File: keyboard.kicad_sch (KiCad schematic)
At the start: 27 parts, among them J2 Conn_01x05_Pin, SW1 SW_Push, U1 STM32F072C8Tx, U2 74AHCT1G125, U3 XC6206PxxxMR, U4 USB6B1

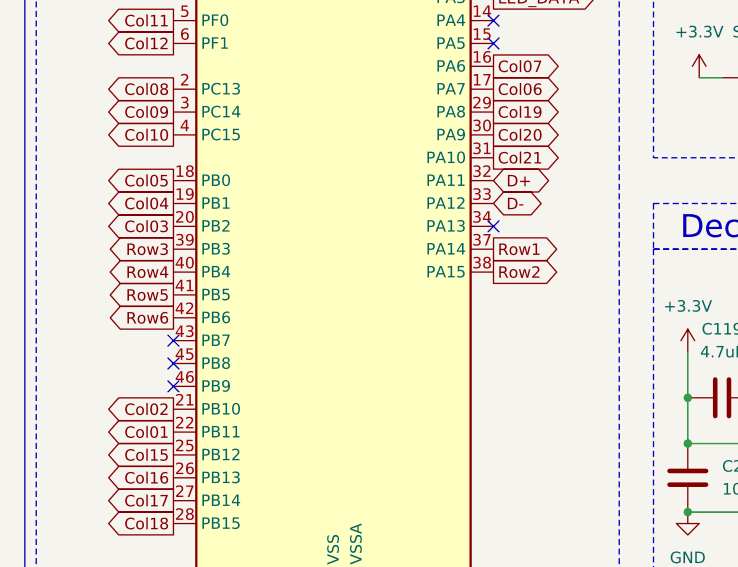
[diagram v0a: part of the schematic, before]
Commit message: Better LED 5V rail setup and matrix wiring
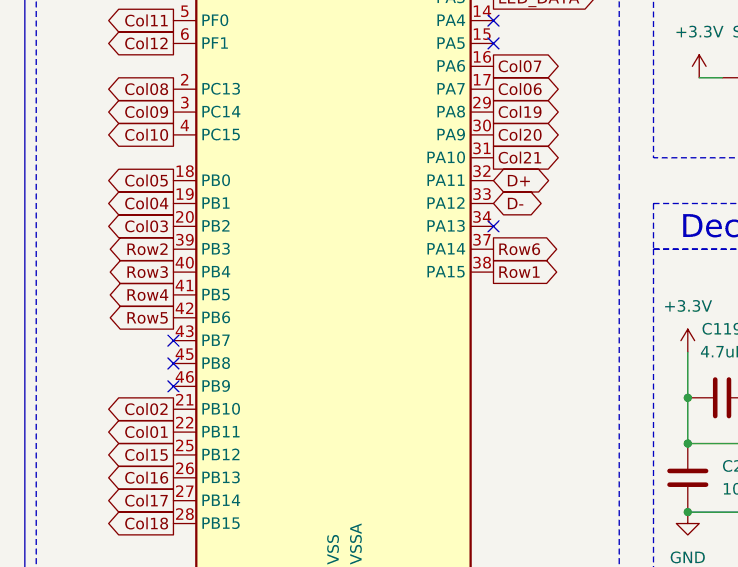
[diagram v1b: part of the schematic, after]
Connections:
- net Row1: now also U1.38 (PA15); no longer U1.37 (PA14)
- net Row2: now also U1.39 (PB3); no longer U1.38 (PA15)
- net Row3: now also U1.40 (PB4); no longer U1.39 (PB3)
- net Row4: now also U1.41 (PB5); no longer U1.40 (PB4)
- net Row5: now also U1.42 (PB6); no longer U1.41 (PB5)
- net Row6: now also U1.37 (PA14); no longer U1.42 (PB6)
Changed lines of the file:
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@@
+		)
+	)
+	(global_label "Row6"
+		(shape output)
+		(at 67.31 83.82 0)
+		(fields_autoplaced yes)
+		(effects
+			(font
+				(size 1.27 1.27)
+			)
+			(justify left)
+		)
+		(property "Intersheetrefs" "${INTERSHEET_REFS}"
+			(at 75.2542 83.82 0)
+			(hide yes)
+			(show_name no)
+			(do_not_autoplace no)
+			(effects
+				(font
+					(size 1.27 1.27)
+				)
+				(justify left)
+			)
 		)
 	)
@@
 		)
 	)
+	(global_label "Row5"
+		(shape output)
+		(at 31.75 91.44 180)
+		(fields_autoplaced yes)
+		(effects
+			(font
+				(size 1.27 1.27)
+			)
+			(justify right)
+		)
+		(property "Intersheetrefs" "${INTERSHEET_REFS}"
+			(at 23.8058 91.44 0)
+			(hide yes)
+			(show_name no)
+			(do_not_autoplace no)
+			(effects
+				(font
+					(size 1.27 1.27)
+				)
+				(justify right)
+			)
+		)
+	)
 	(global_label "Col16"
 		(shape output)
@@
 		)
 	)
+	(global_label "Col06"
+		(shape output)
+		(at 67.31 66.04 0)
+		(fields_autoplaced yes)
+		(effects
+			(font
+				(size 1.27 1.27)
+			)
+			(justify left)
+		)
+		(property "Intersheetrefs" "${INTERSHEET_REFS}"
+			(at 75.7984 66.04 0)
+			(hide yes)
+			(show_name no)
+			(do_not_autoplace no)
+			(effects
+				(font
+					(size 1.27 1.27)
+				)
+				(justify left)
+			)
+		)
+	)
+	(global_label "Col21"
+		(shape input)
+		(at 85.09 151.13 90)
+		(fields_autoplaced yes)
+		(effects
+			(font
+				(size 1.27 1.27)
+			)
+			(justify left)
+		)
+		(property "Intersheetrefs" "${INTERSHEET_REFS}"
+			(at 85.09 142.6416 90)
+			(hide yes)
+			(show_name no)
+			(do_not_autoplace no)
+			(effects
+				(font
+					(size 1.27 1.27)
+				)
+				(justify left)
+			)
+		)
+	)
+	(global_label "Col13"
+		(shape input)
+		(at 64.77 151.13 90)
+		(fields_autoplaced yes)
+		(effects
+			(font
+				(size 1.27 1.27)
+			)
+			(justify left)
+		)
+		(property "Intersheetrefs" "${INTERSHEET_REFS}"
+			(at 64.77 142.6416 90)
+			(hide yes)
+			(show_name no)
+			(do_not_autoplace no)
+			(effects
+				(font
+					(size 1.27 1.27)
+				)
+				(justify left)
+			)
+		)
+	)
 	(global_label "Row1"
 		(shape output)
-		(at 67.31 83.82 0)
-		(fields_autoplaced yes)
-		(effects
-			(font
-				(size 1.27 1.27)
-			)
-			(justify left)
-		)
-		(property "Intersheetrefs" "${INTERSHEET_REFS}"
-			(at 75.2542 83.82 0)
-			(hide yes)
-			(show_name no)
-			(do_not_autoplace no)
-			(effects
-				(font
-					(size 1.27 1.27)
-				)
-				(justify left)
-			)
-		)
-	)
-	(global_label "Col06"
-		(shape output)
-		(at 67.31 66.04 0)
-		(fields_autoplaced yes)
-		(effects
-			(font
-				(size 1.27 1.27)
-			)
-			(justify left)
-		)
-		(property "Intersheetrefs" "${INTERSHEET_REFS}"
-			(at 75.7984 66.04 0)
-			(hide yes)
-			(show_name no)
-			(do_not_autoplace no)
-			(effects
-				(font
-					(size 1.27 1.27)
-				)
-				(justify left)
-			)
-		)
-	)
-	(global_label "Col21"
-		(shape input)
-		(at 85.09 151.13 90)
-		(fields_autoplaced yes)
-		(effects
-			(font
-				(size 1.27 1.27)
-			)
-			(justify left)
-		)
-		(property "Intersheetrefs" "${INTERSHEET_REFS}"
-			(at 85.09 142.6416 90)
-			(hide yes)
-			(show_name no)
-			(do_not_autoplace no)
-			(effects
-				(font
-					(size 1.27 1.27)
-				)
-				(justify left)
-			)
-		)
-	)
-	(global_label "Col13"
-		(shape input)
-		(at 64.77 151.13 90)
-		(fields_autoplaced yes)
-		(effects
-			(font
-				(size 1.27 1.27)
-			)
-			(justify left)
-		)
-		(property "Intersheetrefs" "${INTERSHEET_REFS}"
-			(at 64.77 142.6416 90)
-			(hide yes)
-			(show_name no)
-			(do_not_autoplace no)
-			(effects
-				(font
-					(size 1.27 1.27)
-				)
-				(justify left)
+		(at 67.31 86.36 0)
+		(fields_autoplaced yes)
+		(effects
+			(font
+				(size 1.27 1.27)
+			)
+			(justify left)
+		)
+		(property "Intersheetrefs" "${INTERSHEET_REFS}"
+			(at 75.2542 86.36 0)
+			(hide yes)
+			(show_name no)
+			(do_not_autoplace no)
+			(effects
+				(font
+					(size 1.27 1.27)
+				)
+				(justify left)
+			)
+		)
+	)
+	(global_label "Row2"
+		(shape output)
+		(at 31.75 83.82 180)
+		(fields_autoplaced yes)
+		(effects
+			(font
+				(size 1.27 1.27)
+			)
+			(justify right)
+		)
+		(property "Intersheetrefs" "${INTERSHEET_REFS}"
+			(at 23.8058 83.82 0)
+			(hide yes)
+			(show_name no)
+			(do_not_autoplace no)
+			(effects
+				(font
+					(size 1.27 1.27)
+				)
+				(justify right)
 			)
 		)
@@
 		)
 	)
-	(global_label "Row2"
-		(shape output)
-		(at 67.31 86.36 0)
-		(fields_autoplaced yes)
-		(effects
-			(font
-				(size 1.27 1.27)
-			)
-			(justify left)
-		)
-		(property "Intersheetrefs" "${INTERSHEET_REFS}"
-			(at 75.2542 86.36 0)
-			(hide yes)
-			(show_name no)
-			(do_not_autoplace no)
-			(effects
-				(font
-					(size 1.27 1.27)
-				)
-				(justify left)
-			)
-		)
-	)
 	(global_label "LED"
 		(shape output)
@@
 		(property "Intersheetrefs" "${INTERSHEET_REFS}"
 			(at 23.2616 111.76 0)
-			(hide yes)
-			(show_name no)
-			(do_not_autoplace no)
-			(effects
-				(font
-					(size 1.27 1.27)
-				)
-				(justify right)
-			)
-		)
-	)
-	(global_label "Row5"
-		(shape output)
-		(at 31.75 88.9 180)
-		(fields_autoplaced yes)
-		(effects
-			(font
-				(size 1.27 1.27)
-			)
-			(justify right)
-		)
-		(property "Intersheetrefs" "${INTERSHEET_REFS}"
-			(at 23.8058 88.9 0)
 			(hide yes)
 			(show_name no)
@@
 		)
 	)
-	(global_label "Row6"
-		(shape output)
-		(at 31.75 91.44 180)
-		(fields_autoplaced yes)
-		(effects
-			(font
-				(size 1.27 1.27)
-			)
-			(justify right)
-		)
-		(property "Intersheetrefs" "${INTERSHEET_REFS}"
-			(at 23.8058 91.44 0)
+	(global_label "Row4"
+		(shape output)
+		(at 31.75 88.9 180)
+		(fields_autoplaced yes)
+		(effects
+			(font
+				(size 1.27 1.27)
+			)
+			(justify right)
+		)
+		(property "Intersheetrefs" "${INTERSHEET_REFS}"
+			(at 23.8058 88.9 0)
 			(hide yes)
 			(show_name no)
@@
 		(property "Intersheetrefs" "${INTERSHEET_REFS}"
 			(at 23.8662 53.34 0)
-			(hide yes)
-			(show_name no)
-			(do_not_autoplace no)
-			(effects
-				(font
-					(size 1.27 1.27)
-				)
-				(justify right)
-			)
-		)
-	)
-	(global_label "Row3"
-		(shape output)
-		(at 31.75 83.82 180)
-		(fields_autoplaced yes)
-		(effects
-			(font
-				(size 1.27 1.27)
-			)
-			(justify right)
-		)
-		(property "Intersheetrefs" "${INTERSHEET_REFS}"
-			(at 23.8058 83.82 0)
 			(hide yes)
 			(show_name no)
@@
 		)
 	)
-	(global_label "Row4"
-		(shape output)
-		(at 31.75 86.36 180)
-		(fields_autoplaced yes)
-		(effects
-			(font
-				(size 1.27 1.27)
-			)
-			(justify right)
-		)
-		(property "Intersheetrefs" "${INTERSHEET_REFS}"
-			(at 23.8058 86.36 0)
-			(hide yes)
-			(show_name no)
-			(do_not_autoplace no)
-			(effects
-				(font
-					(size 1.27 1.27)
-				)
-				(justify right)
-			)
-		)
-	)
 	(global_label "Row2"
 		(shape input)
@@
 			(hide yes)
 			(show_name no)
+			(do_not_autoplace no)
+			(effects
+				(font
+					(size 1.27 1.27)
+				)
+				(justify right)
+			)
+		)
+	)
+	(global_label "Row3"
+		(shape output)
+		(at 31.75 86.36 180)
+		(fields_autoplaced yes)
+		(effects
+			(font
+				(size 1.27 1.27)
+			)
+			(justify right)
+		)
+		(property "Intersheetrefs" "${INTERSHEET_REFS}"
+			(at 23.8058 86.36 0)
+			(hide yes)
+			(show_name no)

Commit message: JLCPCB production files and BOM
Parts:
- R1, R4: value 5.1k -> 5.1K
- R2: value 470 -> 470R
- renumbered J2 to J1
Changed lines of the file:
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@@
 			)
 		)
-		(property "Value" "470"
+		(property "Value" "470R"
 			(at 148.844 176.276 90)
 			(show_name no)
@@
 		(in_pos_files yes)
 		(dnp no)
-		(property "Reference" "J2"
+		(property "Reference" "J1"
 			(at 194.31 55.88 0)
 			(show_name no)
@@
 			(project "keyboard"
 				(path "/16cf91c7-4491-4cad-ace1-664941c2385a"
-					(reference "J2")
+					(reference "J1")
 					(unit 1)
 				)
@@
 			)
 		)
-		(property "Value" "5.1k"
+		(property "Value" "5.1K"
 			(at 118.11 60.96 90)
 			(show_name no)
@@
 			)
 		)
-		(property "Value" "5.1k"
+		(property "Value" "5.1K"
 			(at 110.49 60.96 90)
 			(show_name no)

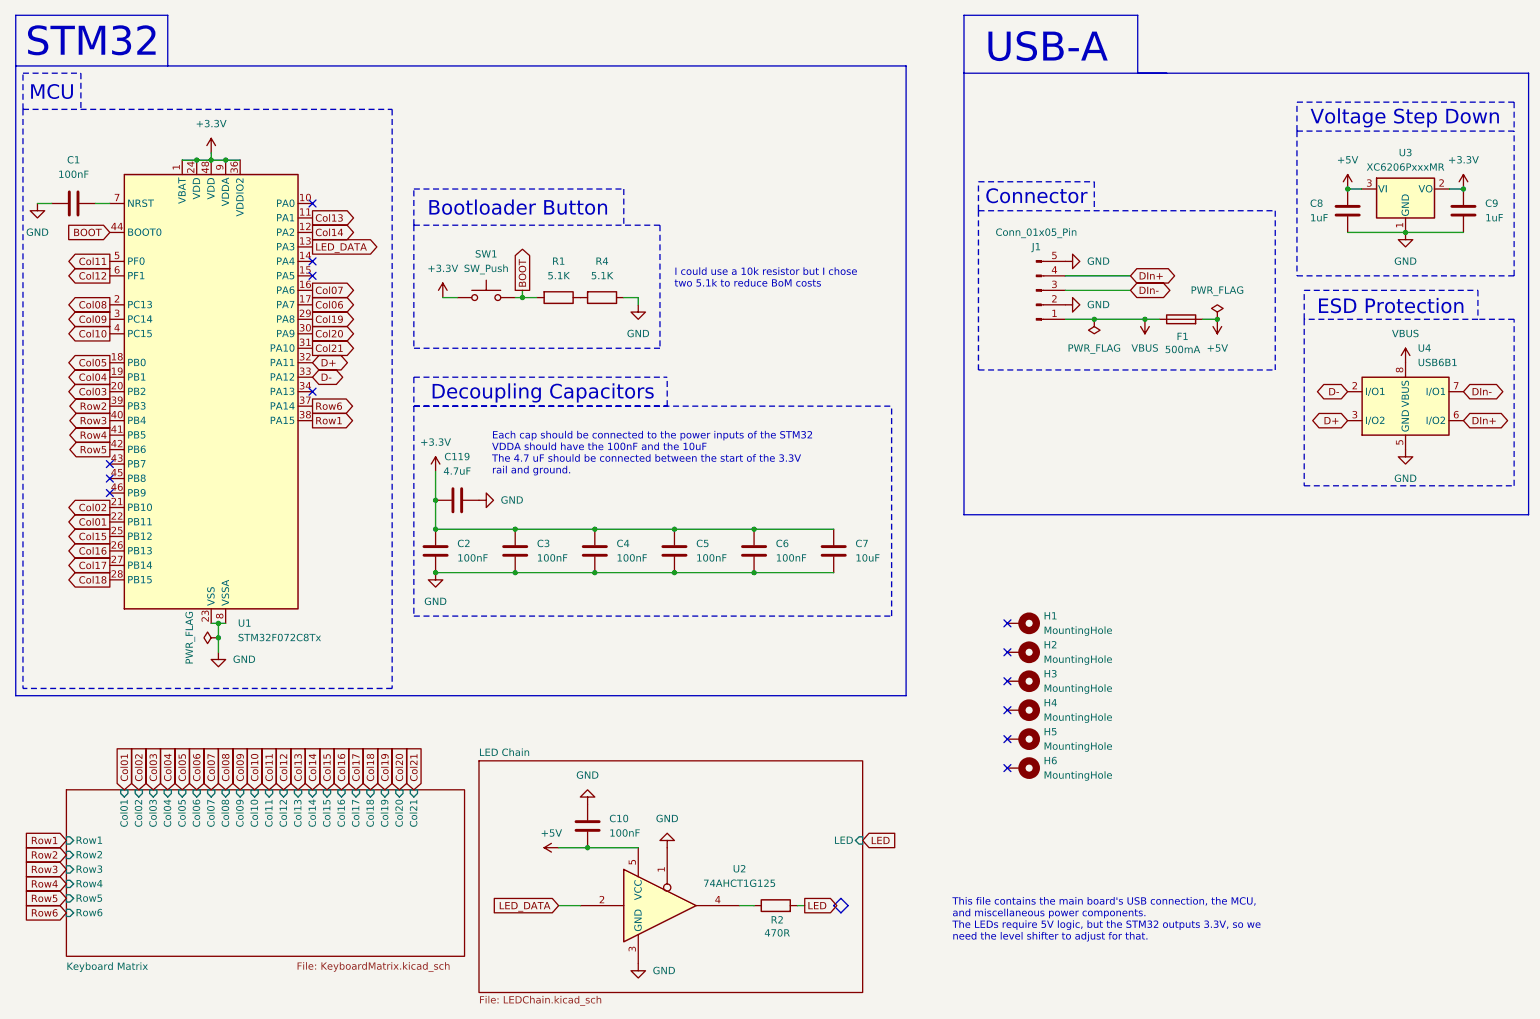
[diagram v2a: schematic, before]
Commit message: USB differential pair mistake correction. Oh dear. Guess this is the start of Rev 2 now.
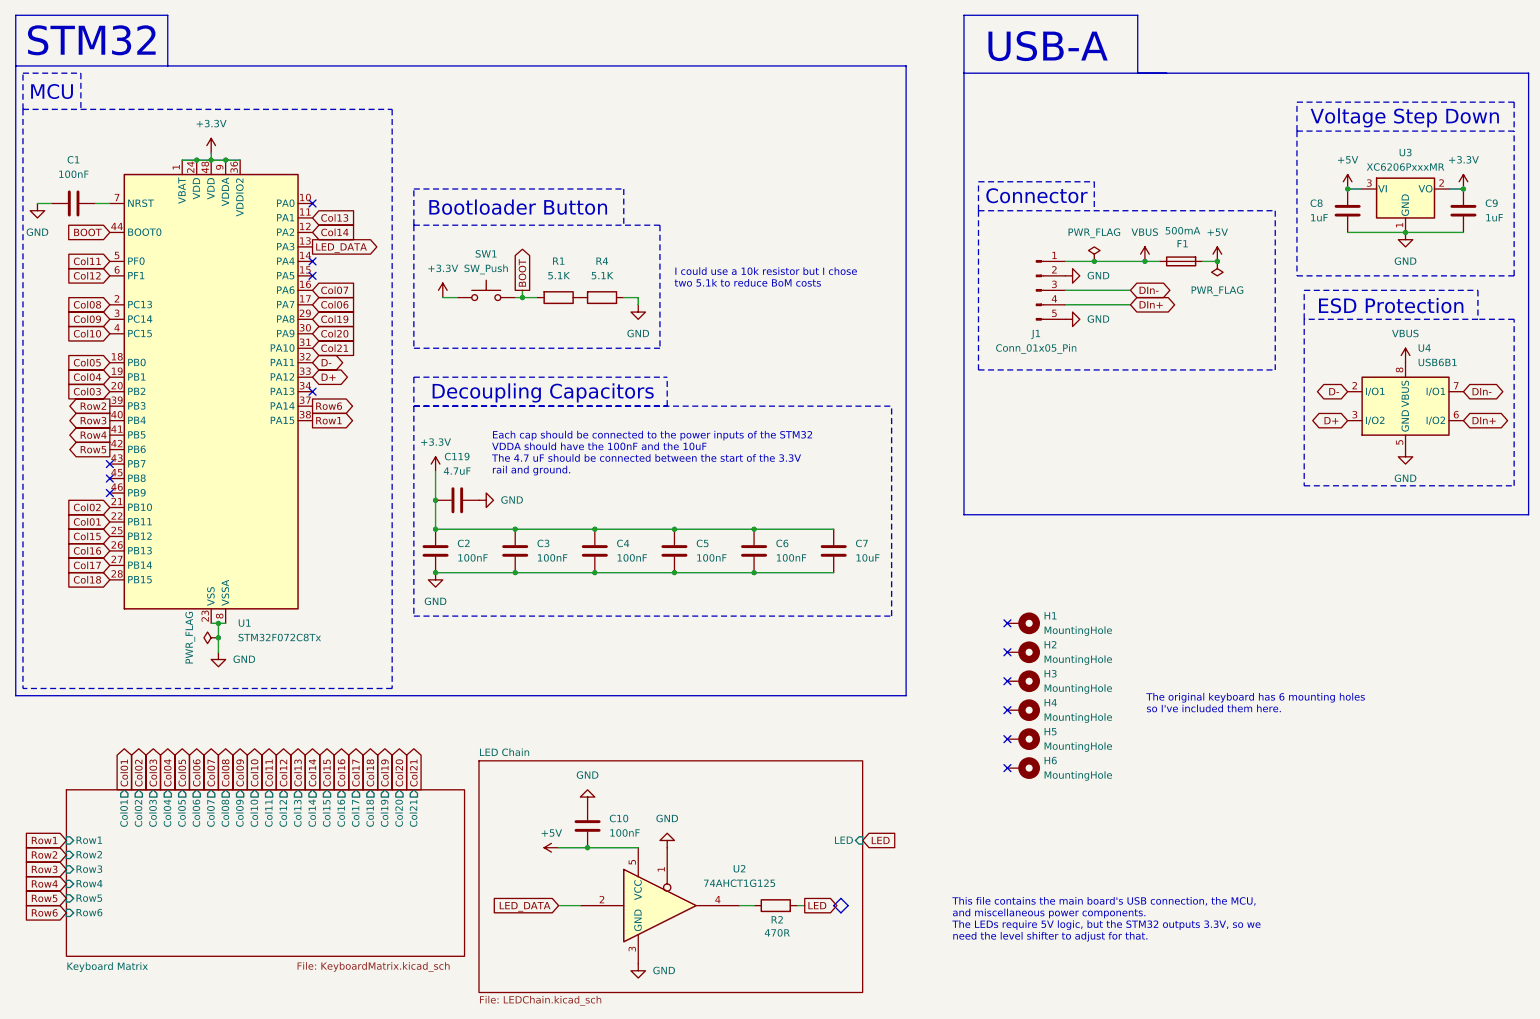
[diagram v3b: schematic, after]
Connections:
- net D+: now also U1.33 (PA12); no longer U1.32 (PA11)
- net D-: now also U1.32 (PA11); no longer U1.33 (PA12)
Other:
- note added: "The original keyboard has 6 mounting holes so I've included them here."
- moved on the sheet: F1

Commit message: Revision 2
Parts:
- C8, C9: footprint Capacitor_SMD:C_0402_1005Metric -> Capacitor_SMD:C_0603_1608Metric
